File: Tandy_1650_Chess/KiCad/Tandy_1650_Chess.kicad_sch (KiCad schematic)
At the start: 147 parts, among them Q1 KSA992, Q2 KSA992, SW1 A8, SW10 B7, SW11 C7, SW12 D7, SW13 E7, SW14 F7, SW15 G7, SW16 H7, SW17 A6, SW18 B6, SW19 C6, SW2 B8, SW20 D6, SW21 E6, SW22 F6, SW23 G6, SW24 H6, SW25 A5, SW26 B5, SW27 C5, SW28 D5, SW29 E5, SW3 C8, SW30 F5, SW31 G5, SW32 H5, SW33 A4, SW34 B4, SW35 C4, SW36 D4, SW37 E4, SW38 F4, SW39 G4, SW4 D8, SW40 H4, SW41 A3, SW42 B3, SW43 C3, SW44 D3, SW45 E3, SW46 F3, SW47 G3, SW48 H3, SW49 A2, SW5 E8, SW50 B2, SW51 C2, SW52 D2, SW53 E2, SW54 F2, SW55 G2, SW56 H2, SW57 A1, SW58 B1, SW59 C1, SW6 F8, SW60 D1, SW61 E1, SW62 F1, SW63 G1, SW64 H1, SW65 COLOUR, SW66 NEW GAME, SW67 2ndF, SW68 KING, SW69 ROOK, SW7 G8, SW70 BISHOP, SW71 TAKE BACK, SW72 LEVEL, SW73 PLAY, SW74 KNIGHT, SW75 PAWN, SW76 QUEEN, SW77 ACL, SW78 POWER, SW8 H8, SW9 A7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

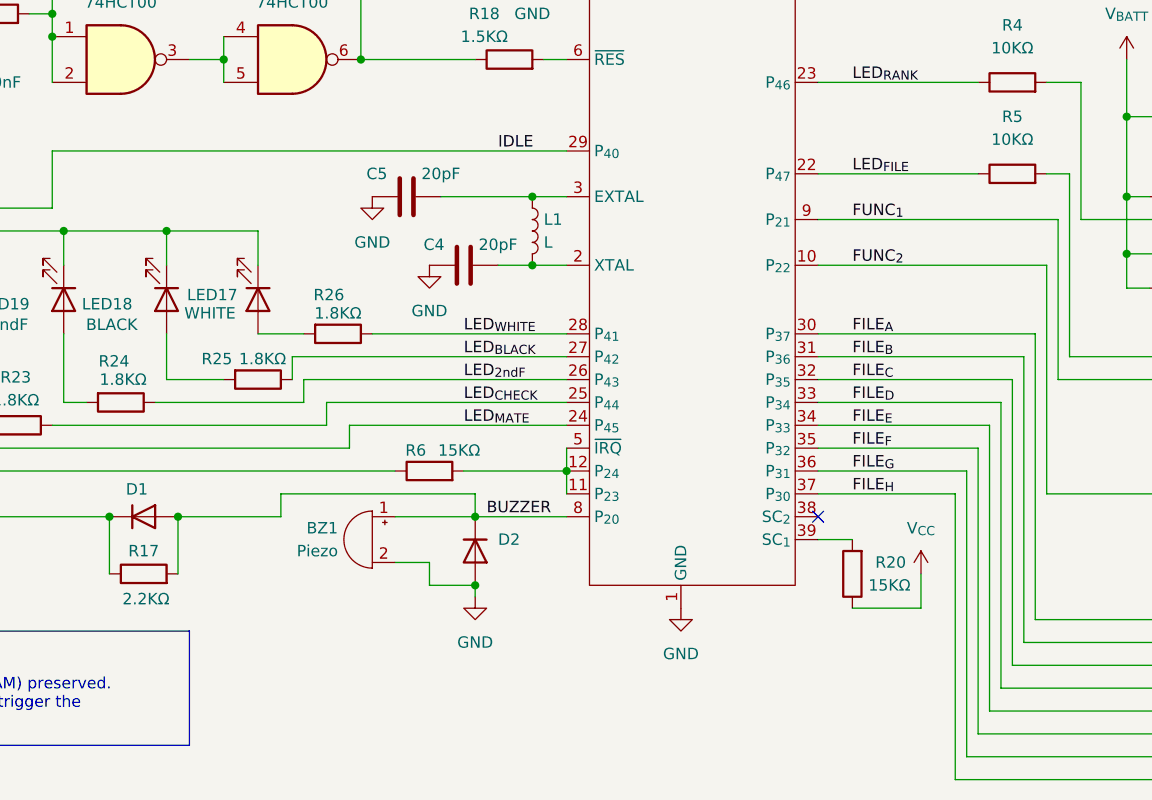
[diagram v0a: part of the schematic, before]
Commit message: Added estimated L1 inductance
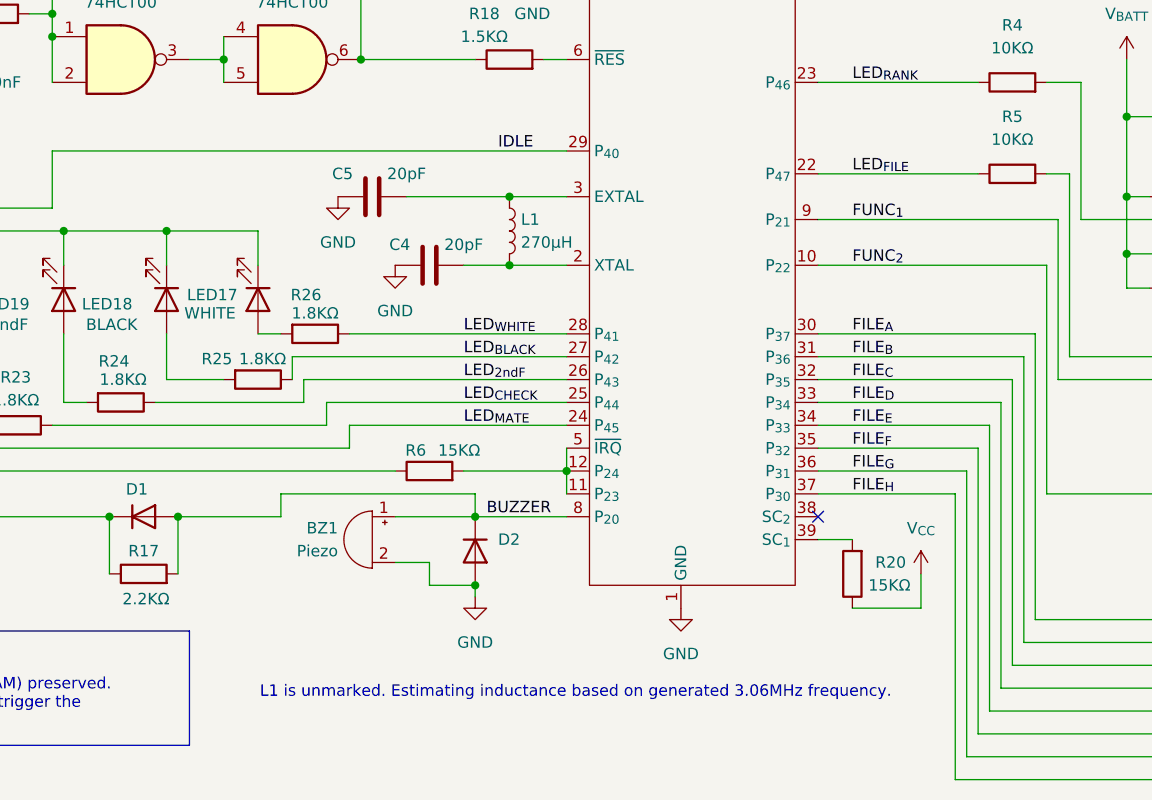
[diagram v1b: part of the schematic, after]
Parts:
- L1: value L -> 270µH
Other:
- note added: "L1 is unmarked. Estimating inductance based on generated 3.06MHz frequency."
- moved on the sheet: C4, C5, L1, R26
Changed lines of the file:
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@@
 		)
 	)
+	(text "L1 is unmarked. Estimating inductance based on generated 3.06MHz frequency."
+		(exclude_from_sim no)
+		(at 139.446 220.218 0)
+		(effects
+			(font
+				(size 1.27 1.27)
+			)
+		)
+	)
 	(text "MCU is SciSys TE-1\nROM code 0609V171\nHitachi HD6301V"
 		(exclude_from_sim no)
@@
 	)
 	(junction
+		(at 132.08 165.1)
+		(diameter 0)
+		(color 0 0 0 0)
+	)
+	(junction
 		(at 275.59 99.06)
 		(diameter 0)
@@
 	)
 	(junction
+		(at 132.08 172.72)
+		(diameter 0)
+		(color 0 0 0 0)
+	)
+	(junction
 		(at 292.1 60.96)
 		(diameter 0)
@@
 	)
 	(junction
-		(at 134.62 165.1)
-		(diameter 0)
-		(color 0 0 0 0)
-	)
-	(junction
 		(at 275.59 60.96)
 		(diameter 0)
@@
 	)
 	(junction
-		(at 134.62 172.72)
-		(diameter 0)
-		(color 0 0 0 0)
-	)
-	(junction
 		(at 341.63 73.66)
 		(diameter 0)
@@
 	(wire
 		(pts
-			(xy 138.43 180.34) (xy 116.84 180.34)
+			(xy 138.43 180.34) (xy 114.3 180.34)
 		)
 		(stroke
@@
 	(wire
 		(pts
-			(xy 124.46 165.1) (xy 134.62 165.1)
+			(xy 120.65 165.1) (xy 132.08 165.1)
 		)
 		(stroke
@@
 	(wire
 		(pts
+			(xy 132.08 165.1) (xy 138.43 165.1)
+		)
+		(stroke
+			(width 0)
+			(type default)
+		)
+	)
+	(wire
+		(pts
 			(xy 116.84 68.58) (xy 116.84 66.04)
 		)
@@
 	(wire
 		(pts
-			(xy 104.14 180.34) (xy 109.22 180.34)
+			(xy 104.14 180.34) (xy 106.68 180.34)
 		)
 		(stroke
@@
 	(wire
 		(pts
+			(xy 132.08 172.72) (xy 138.43 172.72)
+		)
+		(stroke
+			(width 0)
+			(type default)
+		)
+	)
+	(wire
+		(pts
 			(xy 81.28 144.78) (xy 81.28 137.16)
 		)
@@
 	(wire
 		(pts
-			(xy 134.62 172.72) (xy 138.43 172.72)
-		)
-		(stroke
-			(width 0)
-			(type default)
-		)
-	)
-	(wire
-		(pts
 			(xy 109.22 185.42) (xy 138.43 185.42)
 		)
@@
 	(wire
 		(pts
-			(xy 130.81 172.72) (xy 134.62 172.72)
+			(xy 127 172.72) (xy 132.08 172.72)
 		)
 		(stroke
@@
 	(wire
 		(pts
-			(xy 134.62 165.1) (xy 138.43 165.1)
-		)
-		(stroke
-			(width 0)
-			(type default)
-		)
-	)
-	(wire
-		(pts
 			(xy 297.18 185.42) (xy 313.69 185.42)
 		)
@@
 	(symbol
 		(lib_id "Device:C")
-		(at 127 172.72 90)
+		(at 123.19 172.72 90)
 		(unit 1)
 		(exclude_from_sim no)
@@
 		(dnp no)
 		(property "Reference" "C4"
-			(at 123.698 170.434 90)
+			(at 119.888 170.434 90)
 			(effects
 				(font
@@
 		)
 		(property "Value" "20pF"
-			(at 130.81 170.434 90)
+			(at 127 170.434 90)
 			(effects
 				(font
@@
 		)
 		(property "Footprint" ""
-			(at 130.81 171.7548 0)
+			(at 127 171.7548 0)
 			(effects
 				(font
@@
 		)
 		(property "Datasheet" "~"
-			(at 127 172.72 0)
+			(at 123.19 172.72 0)
 			(effects
 				(font
@@
 		)
 		(property "Description" "Unpolarized capacitor"
-			(at 127 172.72 0)
+			(at 123.19 172.72 0)
 			(effects
 				(font
@@
 	(symbol
 		(lib_id "power:GND")
-		(at 123.19 172.72 0)
+		(at 119.38 172.72 0)
 		(unit 1)
 		(exclude_from_sim no)
@@
 		(fields_autoplaced yes)
 		(property "Reference" "#PWR04"
-			(at 123.19 179.07 0)
+			(at 119.38 179.07 0)
 			(effects
 				(font
@@
 		)
 		(property "Value" "GND"
-			(at 123.19 177.8 0)
+			(at 119.38 177.8 0)
 			(effects
 				(font
@@
 		)
 		(property "Footprint" ""
-			(at 123.19 172.72 0)
+			(at 119.38 172.72 0)
 			(effects
 				(font
@@
 		)
 		(property "Datasheet" ""
-			(at 123.19 172.72 0)
+			(at 119.38 172.72 0)
 			(effects
 				(font
@@
 		)
 		(property "Description" "Power symbol creates a global label with name \"GND\" , ground"
-			(at 123.19 172.72 0)
+			(at 119.38 172.72 0)
 			(effects
 				(font
@@
 	(symbol
 		(lib_id "power:GND")
-		(at 116.84 165.1 0)
+		(at 113.03 165.1 0)
 		(unit 1)
 		(exclude_from_sim no)
@@
 		(fields_autoplaced yes)
 		(property "Reference" "#PWR03"
-			(at 116.84 171.45 0)
+			(at 113.03 171.45 0)
 			(effects
 				(font
@@
 		)
 		(property "Value" "GND"
-			(at 116.84 170.18 0)
+			(at 113.03 170.18 0)
 			(effects
 				(font
@@
 		)
 		(property "Footprint" ""
-			(at 116.84 165.1 0)
+			(at 113.03 165.1 0)
 			(effects
 				(font
@@
 		)
 		(property "Datasheet" ""
-			(at 116.84 165.1 0)
+			(at 113.03 165.1 0)
 			(effects
 				(font
@@
 		)
 		(property "Description" "Power symbol creates a global label with name \"GND\" , ground"
-			(at 116.84 165.1 0)
+			(at 113.03 165.1 0)
 			(effects
 				(font
@@
 	(symbol
 		(lib_id "Device:L")
-		(at 134.62 168.91 0)
+		(at 132.08 168.91 0)
 		(unit 1)
 		(exclude_from_sim no)
@@
 		(fields_autoplaced yes)
 		(property "Reference" "L1"
-			(at 135.89 167.6399 0)
+			(at 133.35 167.6399 0)
 			(effects
 				(font
@@
 			)
 		)
-		(property "Value" "L"
-			(at 135.89 170.1799 0)
+		(property "Value" "270µH"
+			(at 133.35 170.1799 0)
 			(effects
 				(font
@@
 		)
 		(property "Footprint" ""
-			(at 134.62 168.91 0)
+			(at 132.08 168.91 0)
 			(effects
 				(font
@@
 		)
 		(property "Datasheet" "~"
-			(at 134.62 168.91 0)
+			(at 132.08 168.91 0)
 			(effects
 				(font
@@
 		)
 		(property "Description" "Inductor"
-			(at 134.62 168.91 0)
+			(at 132.08 168.91 0)
 			(effects
 				(font
@@
 	(symbol
 		(lib_id "Device:C")
-		(at 120.65 165.1 90)
+		(at 116.84 165.1 90)
 		(unit 1)
 		(exclude_from_sim no)
@@
 		(dnp no)
 		(property "Reference" "C5"
-			(at 117.348 162.56 90)
+			(at 113.538 162.56 90)
 			(effects
 				(font
@@
 		)
 		(property "Value" "20pF"
-			(at 124.46 162.56 90)
+			(at 120.65 162.56 90)
 			(effects
 				(font
@@
 		)
 		(property "Footprint" ""
-			(at 124.46 164.1348 0)
+			(at 120.65 164.1348 0)
 			(effects
 				(font
@@
 		)
 		(property "Datasheet" "~"
-			(at 120.65 165.1 0)
+			(at 116.84 165.1 0)
 			(effects
 				(font
@@
 		)
 		(property "Description" "Unpolarized capacitor"
-			(at 120.65 165.1 0)
+			(at 116.84 165.1 0)
 			(effects
 				(font
@@
 	(symbol
 		(lib_id "Device:R")
-		(at 113.03 180.34 270)
+		(at 110.49 180.34 270)
 		(unit 1)
 		(exclude_from_sim no)
@@
 		(dnp no)
 		(property "Reference" "R26"
-			(at 112.014 176.022 90)
+			(at 109.474 176.022 90)
 			(effects
 				(font
@@
 		)
 		(property "Value" "1.8KΩ"
-			(at 113.03 178.054 90)
+			(at 110.49 178.054 90)
 			(effects
 				(font
@@
 		)
 		(property "Footprint" ""
-			(at 113.03 178.562 90)
+			(at 110.49 178.562 90)
 			(effects
 				(font
@@
 		)
 		(property "Datasheet" "~"
-			(at 113.03 180.34 0)
+			(at 110.49 180.34 0)
 			(effects
 				(font
@@
 		)
 		(property "Description" "Resistor"
-			(at 113.03 180.34 0)
+			(at 110.49 180.34 0)
 			(effects
 				(font

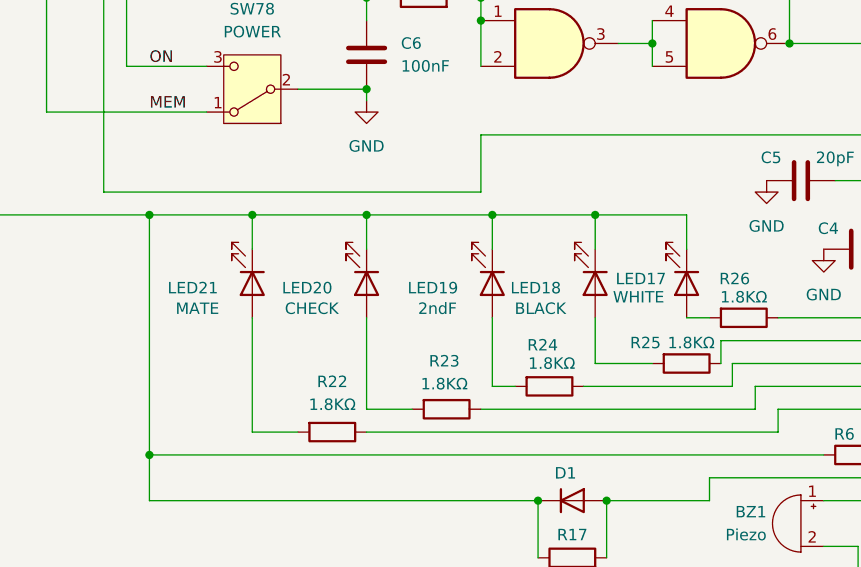
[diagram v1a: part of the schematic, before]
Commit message: Corrected function LED orientation
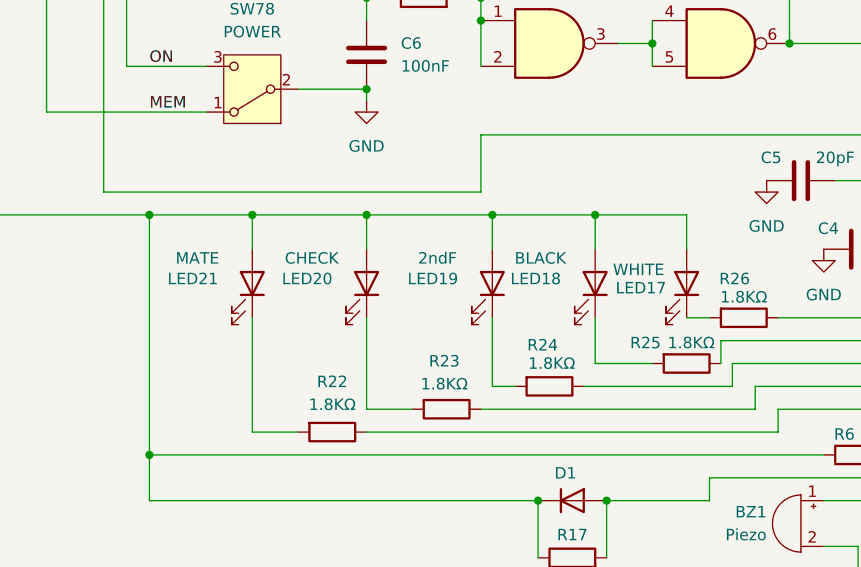
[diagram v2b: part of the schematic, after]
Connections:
- net V_{CC}: now also LED17.2 (A), LED18.2 (A), LED19.2 (A), LED20.2 (A), LED21.2 (A); no longer LED17.1 (K), LED18.1 (K), LED19.1 (K), LED20.1 (K), LED21.1 (K)
- net at R25.2: now also LED18.1 (K); no longer LED18.2 (A)
- net at R26.2: now also LED17.1 (K); no longer LED17.2 (A)
- net at R23.2: now also LED20.1 (K); no longer LED20.2 (A)
- net at R24.2: now also LED19.1 (K); no longer LED19.2 (A)
- net at R22.2: now also LED21.1 (K); no longer LED21.2 (A)
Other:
- moved on the sheet: LED17, LED18, LED19, LED20, LED21
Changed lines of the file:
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@@
 		(lib_id "Device:LED")
 		(at 93.98 176.53 270)
+		(mirror x)
 		(unit 1)
 		(exclude_from_sim no)
@@
 		(dnp no)
 		(property "Reference" "LED18"
-			(at 87.376 177.038 90)
+			(at 87.376 176.022 90)
 			(effects
 				(font
@@
 		)
 		(property "Value" "BLACK"
-			(at 87.884 179.324 90)
+			(at 87.884 173.736 90)
 			(effects
 				(font
@@
 		(lib_id "Device:LED")
 		(at 104.14 176.53 270)
+		(mirror x)
 		(unit 1)
 		(exclude_from_sim no)
@@
 		(dnp no)
 		(property "Reference" "LED17"
-			(at 99.06 176.022 90)
+			(at 99.06 177.038 90)
 			(effects
 				(font
@@
 		)
 		(property "Value" "WHITE"
-			(at 98.806 178.054 90)
+			(at 98.806 175.006 90)
 			(effects
 				(font
@@
 		(lib_id "Device:LED")
 		(at 82.55 176.53 270)
+		(mirror x)
 		(unit 1)
 		(exclude_from_sim no)
@@
 		(dnp no)
 		(property "Reference" "LED19"
-			(at 75.946 177.038 90)
+			(at 75.946 176.022 90)
 			(effects
 				(font
@@
 		)
 		(property "Value" "2ndF"
-			(at 76.454 179.324 90)
+			(at 76.454 173.736 90)
 			(effects
 				(font
@@
 		(lib_id "Device:LED")
 		(at 55.88 176.53 270)
+		(mirror x)
 		(unit 1)
 		(exclude_from_sim no)
@@
 		(dnp no)
 		(property "Reference" "LED21"
-			(at 49.276 177.038 90)
+			(at 49.276 176.022 90)
 			(effects
 				(font
@@
 		)
 		(property "Value" "MATE"
-			(at 49.784 179.324 90)
+			(at 49.784 173.736 90)
 			(effects
 				(font
@@
 		(lib_id "Device:LED")
 		(at 68.58 176.53 270)
+		(mirror x)
 		(unit 1)
 		(exclude_from_sim no)
@@
 		(dnp no)
 		(property "Reference" "LED20"
-			(at 61.976 177.038 90)
+			(at 61.976 176.022 90)
 			(effects
 				(font
@@
 		)
 		(property "Value" "CHECK"
-			(at 62.484 179.324 90)
+			(at 62.484 173.736 90)
 			(effects
 				(font
